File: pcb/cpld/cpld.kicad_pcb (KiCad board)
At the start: 2 copper layers, 104.4 x 82.7 mm, 32 parts, among them J1 Micro_SD_Card_Det1, J2 Bus_ISA_8bit_AB_Rev0, J3 Atmel-JTAG-10, SW1 ADDR SEL, U1 ATF1504AS-xJx44, U2 AMS1117-3.3, U3 74LVC125, U4 74HCT688, X1 16MHz

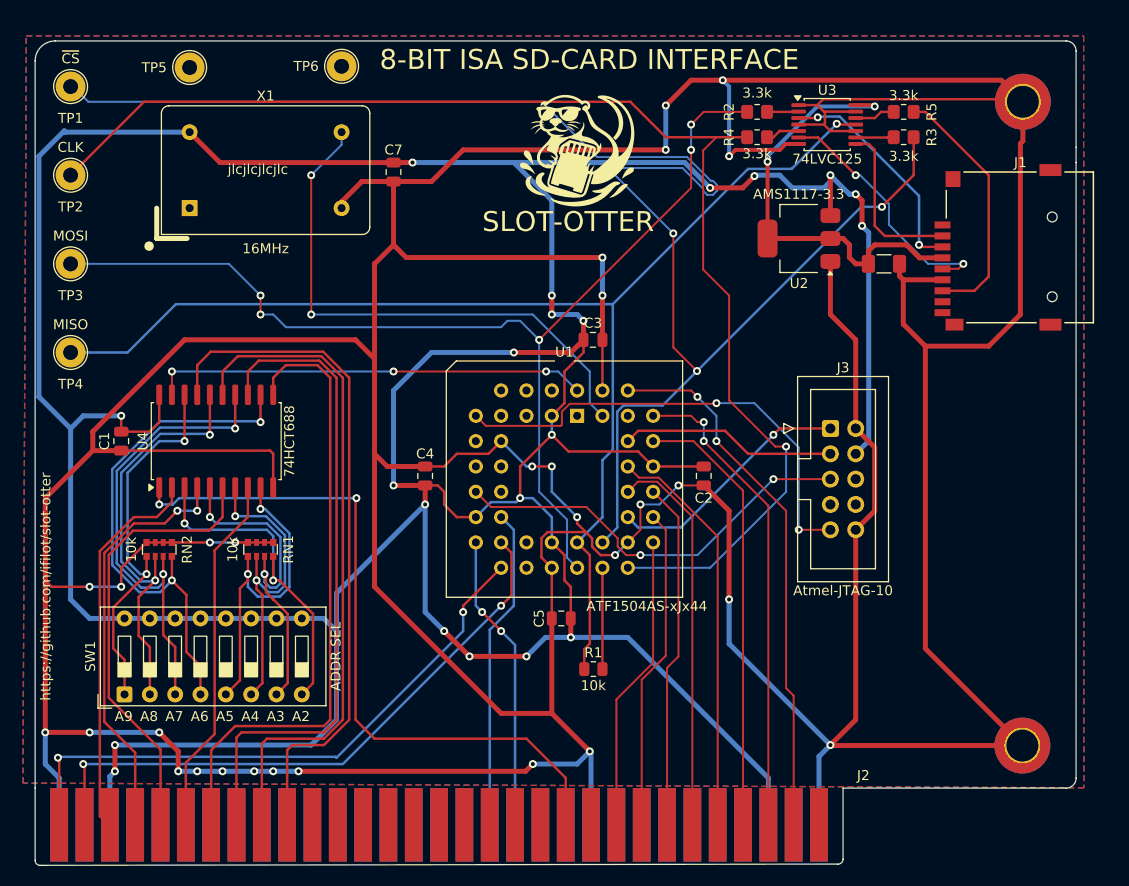
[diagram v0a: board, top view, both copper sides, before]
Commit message: Redesigning CPLD PCB
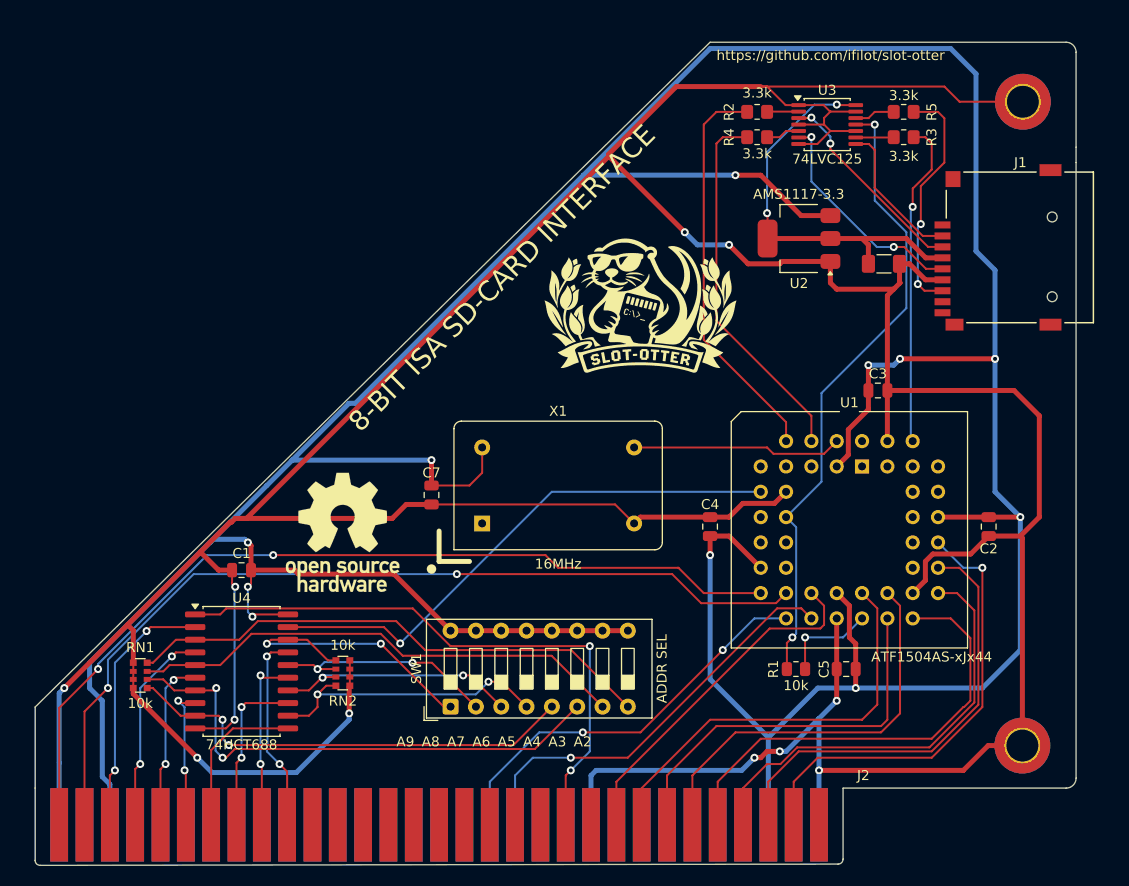
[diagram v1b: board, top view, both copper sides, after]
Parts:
- removed G***: LOGO, components:slototter-logo
- removed J3: Atmel-JTAG-10, Connector_IDC:IDC-Header_2x05_P2.54mm_Vertical
- removed TP1: ~{CS}, TestPoint:TestPoint_Loop_D2.54mm_Drill1.5mm_Beaded
- removed TP2: CLK, TestPoint:TestPoint_Loop_D2.54mm_Drill1.5mm_Beaded
- removed TP3: MOSI, TestPoint:TestPoint_Loop_D2.54mm_Drill1.5mm_Beaded
- removed TP4: MISO, TestPoint:TestPoint_Loop_D2.54mm_Drill1.5mm_Beaded
- removed TP5, TP6: GND, TestPoint:TestPoint_Loop_D2.54mm_Drill1.5mm_Beaded
- added SYM1: ~, components:slototter-logo-v2, F.Cu at (137.4, 64.6)
- added SYM2: ~, Symbol:OSHW-Logo_11.4x12mm_SilkScreen, F.Cu at (107.5, 86.9)
- moved X1 43.1 mm to (121.5, 86.0)
- moved SW1 32.7 mm to (118.4, 104.3)
- moved C7 32.6 mm to (116.4, 83.1)
- moved C3 29.0 mm to (161.2, 72.6)
- moved U1 29.0 mm to (159.6, 80.2)
- moved C2 29.0 mm to (172.3, 86.3)
- moved C4 29.0 mm to (144.4, 86.3)
- moved C5 29.0 mm to (158.0, 100.6)
- moved U4 23.2 mm to (97.4, 100.8), turned to 0 degrees
- moved RN2 22.2 mm to (107.5, 101.0), turned to 180 degrees
- moved R1 20.3 mm to (153.0, 100.6)
- moved C1 17.7 mm to (97.4, 90.6), turned to 0 degrees
- moved RN1 17.5 mm to (87.2, 101.2), turned to 0 degrees
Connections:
- R1 pad 2: Net-(R1-Pad2) -> /MISO_PULL
- U1 pad 12: unconnected-(U1-I/O-Pad12) -> MISO
- U1 pad 13: TMS -> unconnected-(U1-I/O/TMS-Pad13)
- U1 pad 16: ~{RD} -> unconnected-(U1-I/O-Pad16)
- U1 pad 17: ~{WR} -> A0
- U1 pad 18: A0 -> ~{RD}
- U1 pad 2: unconnected-(U1-I/OE2/GCLK2-Pad2) -> 16MHz
- U1 pad 20: unconnected-(U1-I/O-Pad20) -> ~{WR}
- U1 pad 21: unconnected-(U1-I/O-Pad21) -> DB0
- U1 pad 24: MOSI -> /MISO_PULL
- U1 pad 25: MISO -> DB1
- U1 pad 26: Net-(R1-Pad2) -> DB2
- U1 pad 27: ~{CS} -> DB3
- U1 pad 28: CLK -> DB4
- U1 pad 29: DB0 -> DB5
- U1 pad 31: DB1 -> DB6
- U1 pad 32: TCK -> unconnected-(U1-I/O/TCK-Pad32)
- U1 pad 33: DB2 -> DB7
- U1 pad 34: DB3 -> unconnected-(U1-I/O-Pad34)
- U1 pad 36: DB4 -> unconnected-(U1-I/O-Pad36)
- U1 pad 37: DB5 -> unconnected-(U1-I/O-Pad37)
- U1 pad 38: TDO -> unconnected-(U1-I/O/TDO-Pad38)
- U1 pad 39: DB6 -> unconnected-(U1-I/O-Pad39)
- U1 pad 4: unconnected-(U1-I/O-Pad4) -> CLK
- U1 pad 40: DB7 -> ~{CS}
- U1 pad 43: 16MHz -> unconnected-(U1-I/GCLK1-Pad43)
- U1 pad 44: ~{PORTSEL} -> unconnected-(U1-I/OE1-Pad44)
- U1 pad 6: unconnected-(U1-I/O-Pad6) -> MOSI
- U1 pad 7: TDI -> unconnected-(U1-I/O/TDI-Pad7)
- U1 pad 9: unconnected-(U1-I/O-Pad9) -> ~{PORTSEL}
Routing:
- net GND: track 690.0 -> 476.1 mm, vias 29 -> 11
- net ~{CS}: track 163.0 -> 32.9 mm, vias 3 -> 1
- net CLK: track 131.6 -> 37.1 mm, vias 1 -> 0
- net MOSI: track 110.3 -> 40.0 mm, vias 5 -> 0
- net MISO: track 127.1 -> 63.6 mm, vias 1 -> 2
- net A8: track 67.6 -> 18.0 mm, vias 0 -> 2
- net A7: track 66.3 -> 17.0 mm, vias 0 -> 2
- net A9: track 69.3 -> 20.2 mm, vias 0 -> 2
- net TDI: track 47.8 -> 0.00 mm, vias 2 -> 0
- net A6: track 63.6 -> 16.2 mm
- net TMS: track 41.8 -> 0.00 mm, vias 2 -> 0
- net VCC: track 444.7 -> 409.5 mm, vias 21 -> 11
- net 16MHz: track 54.8 -> 21.1 mm, vias 2 -> 0
- net A0: track 60.8 -> 90.4 mm
- net A1: track 62.0 -> 90.8 mm
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- removed copper zone on F.Cu, net GND
- removed copper zone on B.Cu, net VCC
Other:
- board size 104.4 x 82.7 mm -> 104.4 x 82.5 mm
- board text removed: "SLOT-OTTER"
- board text removed: "jlcjlcjlcjlc"

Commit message: Final tweaks CPLD
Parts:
- U1: value ATF1504AS-xJx44 -> ATF1504AS
- moved SYM2 0.67 mm to (108.2, 86.9)
- moved SYM1 0.42 mm to (137.4, 65.0)
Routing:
- net DB5: track 44.2 -> 44.7 mm
- added copper zone on F.Cu, net GND
- added copper zone on B.Cu, net VCC

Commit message: Refactoring for release
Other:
- board text added: "CPLD rev 1.0"
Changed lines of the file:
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@@
 	(paper "A4")
 	(title_block
-		(title "ISA SD CARD")
-		(date "2024-05-26")
-		(rev "rev6")
+		(title "Slot-otter CPLD")
+		(date "2026-10-16")
+		(rev "1.0")
+		(comment 1 "Hardware: CERN-OHL-S-2.0; source: github.com/ifilot/slot-otter")
 	)
 	(layers
@@
 			)
 		)
+		(attr exclude_from_pos_files exclude_from_bom)
 		(duplicate_pad_numbers_are_jumpers no)
 		(fp_poly
@@
 			)
 		)
-		(property "Datasheet" "http://ww1.microchip.com/downloads/en/DeviceDoc/Atmel-0995-CPLD-ATF1502AS(L)-Datasheet.pdf"
+		(property "Datasheet" "https://ww1.microchip.com/downloads/en/DeviceDoc/ATF1504AS(L)-5V-64-Macrocell-CPLD-Data-Sheet-20006580A.pdf"
 			(at 0 0 0)
 			(unlocked yes)
@@
 			)
 		)
-		(attr board_only)
+		(attr board_only exclude_from_pos_files exclude_from_bom)
 		(duplicate_pad_numbers_are_jumpers no)
 		(fp_poly
@@
 		)
 	)
+	(gr_text "CPLD rev 1.0"
+		(at 166 41.8 0)
+		(layer "F.SilkS")
+		(effects
+			(font
+				(size 1 1)
+				(thickness 0.15)
+			)
+		)
+	)
 	(gr_text "8-BIT ISA SD-CARD INTERFACE"
 		(at 109.455 77.075 45)
@@
 		(layer "F.Cu")
 		(hatch none 0.1)
-		(priority 30157)
+		(priority 30156)
 		(attr
 			(teardrop
@@
 		(layer "F.Cu")
 		(hatch none 0.1)
-		(priority 30024)
+		(priority 30192)
 		(attr
 			(teardrop
@@
 		(polygon
 			(pts
-				(xy 125.028648 96.9675) (xy 125.028648 96.4675) (xy 123.664728 95.951948) (xy 123.427648 96.7175)
-				(xy 123.664728 97.483052)
+				(xy 123.436352 96.9675) (xy 123.436352 96.4675) (xy 122.636352 96.795914) (xy 122.6335 96.7175)
+				(xy 122.636352 96.795914)
 			)
 		)
@@
 		(layer "F.Cu")
 		(hatch none 0.1)
-		(priority 30192)
+		(priority 30024)
 		(attr
 			(teardrop
@@
 		(polygon
 			(pts
-				(xy 123.436352 96.9675) (xy 123.436352 96.4675) (xy 122.636352 96.795914) (xy 122.6335 96.7175)
-				(xy 122.636352 96.795914)
+				(xy 121.836352 96.4675) (xy 121.836352 96.9675) (xy 123.200272 97.483052) (xy 123.437352 96.7175)
+				(xy 123.200272 95.951948)
 			)
 		)
@@
 		(polygon
 			(pts
-				(xy 121.836352 96.4675) (xy 121.836352 96.9675) (xy 123.200272 97.483052) (xy 123.437352 96.7175)
-				(xy 123.200272 95.951948)
+				(xy 125.028648 96.9675) (xy 125.028648 96.4675) (xy 123.664728 95.951948) (xy 123.427648 96.7175)
+				(xy 123.664728 97.483052)
 			)
 		)
@@
 		(layer "F.Cu")
 		(hatch none 0.1)
-		(priority 30193)
+		(priority 30026)
 		(attr
 			(teardrop
@@
 		(polygon
 			(pts
-				(xy 125.976352 96.9675) (xy 125.976352 96.4675) (xy 125.176352 96.795914) (xy 125.1735 96.7175)
-				(xy 125.176352 96.795914)
+				(xy 124.376352 96.4675) (xy 124.376352 96.9675) (xy 125.740272 97.483052) (xy 125.977352 96.7175)
+				(xy 125.740272 95.951948)
 			)
 		)
@@
 		(polygon
 			(pts
-				(xy 124.376352 96.4675) (xy 124.376352 96.9675) (xy 125.740272 97.483052) (xy 125.977352 96.7175)
-				(xy 125.740272 95.951948)
+				(xy 127.568648 96.9675) (xy 127.568648 96.4675) (xy 126.204728 95.951948) (xy 125.967648 96.7175)
+				(xy 126.204728 97.483052)
 			)
 		)
@@
 		(layer "F.Cu")
 		(hatch none 0.1)
-		(priority 30026)
+		(priority 30193)
 		(attr
 			(teardrop
@@
 		(polygon
 			(pts
-				(xy 127.568648 96.9675) (xy 127.568648 96.4675) (xy 126.204728 95.951948) (xy 125.967648 96.7175)
-				(xy 126.204728 97.483052)
+				(xy 125.976352 96.9675) (xy 125.976352 96.4675) (xy 125.176352 96.795914) (xy 125.1735 96.7175)
+				(xy 125.176352 96.795914)
 			)
 		)
@@
 		(layer "F.Cu")
 		(hatch none 0.1)
-		(priority 30158)
+		(priority 30157)
 		(attr
 			(teardrop
@@
 		(layer "F.Cu")
 		(hatch none 0.1)
-		(priority 30159)
+		(priority 30158)
 		(attr
 			(teardrop
@@
 		(layer "F.Cu")
 		(hatch none 0.1)
-		(priority 30147)
+		(priority 30146)
 		(attr
 			(teardrop
@@
 		(layer "F.Cu")
 		(hatch none 0.1)
-		(priority 30160)
+		(priority 30159)
 		(attr
 			(teardrop
@@
 		(layer "F.Cu")
 		(hatch none 0.1)
-		(priority 30001)
+		(priority 30160)
 		(attr
 			(teardrop
@@
 		(layer "F.Cu")
 		(hatch none 0.1)
-		(priority 30000)
+		(priority 30147)
 		(attr
 			(teardrop
@@
 		(layer "F.Cu")
 		(hatch none 0.1)
-		(priority 30031)
+		(priority 30032)
 		(attr
 			(teardrop
@@
 		(layer "F.Cu")
 		(hatch none 0.1)
-		(priority 30032)
+		(priority 30031)
 		(attr
 			(teardrop
@@
 		(layer "F.Cu")
 		(hatch none 0.1)
-		(priority 30196)
+		(priority 30034)
 		(attr
 			(teardrop
@@
 		(polygon
 			(pts
-				(xy 131.056352 96.9675) (xy 131.056352 96.4675) (xy 130.256352 96.795914) (xy 130.2535 96.7175)
-				(xy 130.256352 96.795914)
+				(xy 132.648648 96.9675) (xy 132.648648 96.4675) (xy 131.284728 95.951948) (xy 131.047648 96.7175)
+				(xy 131.284728 97.483052)
 			)
 		)
@@
 		(layer "F.Cu")
 		(hatch none 0.1)
-		(priority 30033)
+		(priority 30196)
 		(attr
 			(teardrop
@@
 		(polygon
 			(pts
-				(xy 129.456352 96.4675) (xy 129.456352 96.9675) (xy 130.820272 97.483052) (xy 131.057352 96.7175)
-				(xy 130.820272 95.951948)
+				(xy 131.056352 96.9675) (xy 131.056352 96.4675) (xy 130.256352 96.795914) (xy 130.2535 96.7175)
+				(xy 130.256352 96.795914)
 			)
 		)
@@
 		(layer "F.Cu")
 		(hatch none 0.1)
-		(priority 30034)
+		(priority 30033)
 		(attr
 			(teardrop
@@
 		(polygon
 			(pts
-				(xy 132.648648 96.9675) (xy 132.648648 96.4675) (xy 131.284728 95.951948) (xy 131.047648 96.7175)
-				(xy 131.284728 97.483052)
+				(xy 129.456352 96.4675) (xy 129.456352 96.9675) (xy 130.820272 97.483052) (xy 131.057352 96.7175)
+				(xy 130.820272 95.951948)
 			)
 		)
@@
 		(layer "B.Cu")
 		(hatch none 0.1)
-		(priority 30001)
+		(priority 30034)
 		(attr
 			(teardrop
@@
 		(layer "B.Cu")
 		(hatch none 0.1)
-		(priority 30034)
+		(priority 30035)
 		(attr
 			(teardrop
@@
 		(layer "B.Cu")
 		(hatch none 0.1)
-		(priority 30035)
+		(priority 30036)
 		(attr
 			(teardrop
@@
 		(layer "B.Cu")
 		(hatch none 0.1)
-		(priority 30036)
+		(priority 30037)
 		(attr
 			(teardrop
@@
 		(layer "B.Cu")
 		(hatch none 0.1)
-		(priority 30037)
+		(priority 30038)
 		(attr
 			(teardrop
@@
 		(layer "B.Cu")
 		(hatch none 0.1)
-		(priority 30038)
+		(priority 30039)
 		(attr
 			(teardrop
@@
 		(layer "B.Cu")
 		(hatch none 0.1)
-		(priority 30039)
+		(priority 30040)
 		(attr
 			(teardrop
@@
 		(layer "B.Cu")
 		(hatch none 0.1)
-		(priority 30040)
+		(priority 30041)
 		(attr
 			(teardrop
@@
 		(layer "B.Cu")
 		(hatch none 0.1)
-		(priority 30041)
+		(priority 30042)
 		(attr
 			(teardrop
@@
 		(layer "B.Cu")
 		(hatch none 0.1)
-		(priority 30042)
+		(priority 30043)
 		(attr
 			(teardrop
@@
 		(layer "B.Cu")
 		(hatch none 0.1)
-		(priority 30000)
+		(priority 30005)
 		(attr
 			(teardrop
@@
 		(layer "B.Cu")
 		(hatch none 0.1)
-		(priority 30000)
+		(priority 30072)
 		(attr
 			(teardrop
